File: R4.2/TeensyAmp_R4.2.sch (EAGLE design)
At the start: 81 parts, among them IC5 NCP164CSN330T1G, IC6 PCM1865DBT, IC7 PCM1865DBT

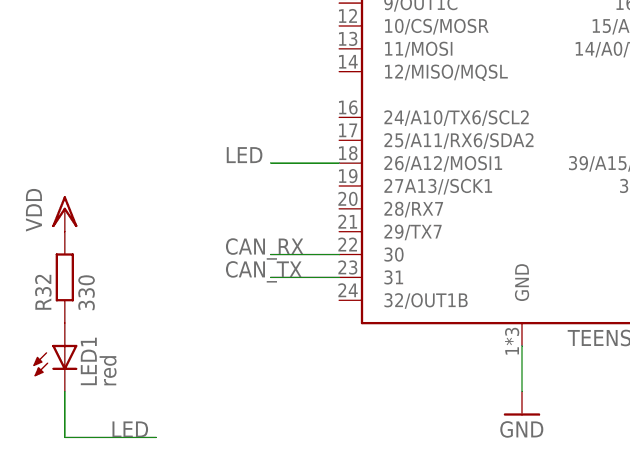
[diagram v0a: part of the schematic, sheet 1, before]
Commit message: [R4.2] LED pin on 27
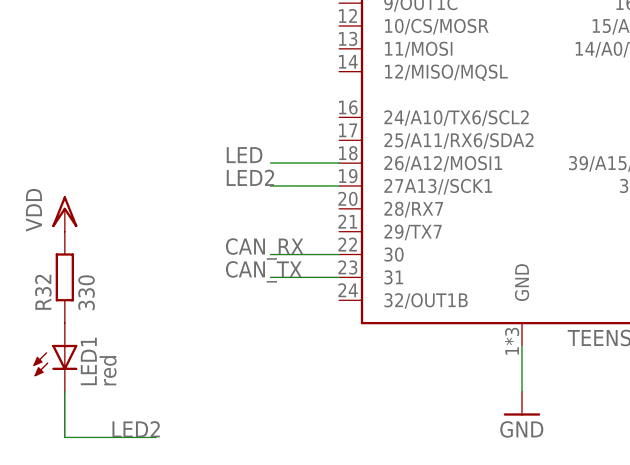
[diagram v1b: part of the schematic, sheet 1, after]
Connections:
- new net LED2: LED1.C, TEENSY4.1.27A13//SCK1
- net LED: no longer LED1.C
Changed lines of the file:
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@@
 <label x="30.48" y="45.72" size="1.778" layer="95"/>
-</segment>
-<segment>
-<pinref part="LED1" gate="G$1" pin="C"/>
-<wire x1="12.7" y1="20.32" x2="12.7" y2="15.24" width="0.1524" layer="91"/>
-<wire x1="12.7" y1="15.24" x2="22.86" y2="15.24" width="0.1524" layer="91"/>
-<label x="17.78" y="15.24" size="1.778" layer="95"/>
 </segment>
 </net>
@@
 </segment>
 </net>
+<net name="LED2" class="0">
+<segment>
+<pinref part="TEENSY4.1" gate="G$1" pin="27A13//SCK1"/>
+<wire x1="43.18" y1="43.18" x2="35.56" y2="43.18" width="0.1524" layer="91"/>
+<label x="30.48" y="43.18" size="1.778" layer="95"/>
+</segment>
+<segment>
+<pinref part="LED1" gate="G$1" pin="C"/>
+<wire x1="12.7" y1="20.32" x2="12.7" y2="15.24" width="0.1524" layer="91"/>
+<wire x1="12.7" y1="15.24" x2="22.86" y2="15.24" width="0.1524" layer="91"/>
+<label x="17.78" y="15.24" size="1.778" layer="95"/>
+</segment>
+</net>
